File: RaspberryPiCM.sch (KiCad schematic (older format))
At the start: 16 parts

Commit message: [modified:] RTC revision [add:] RPis second I2C port
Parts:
- removed C?: 1uF, Capacitor_SMD:C_0603_1608Metric, symbol Device:C
- added C?: 1uF, symbol Device:C
- added C?: 100nF, symbol Device:C
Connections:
- net +3V3: now also C?.1, C?.1
- net Earth: now also C?.2, C?.2; no longer BT?.2 (-), U?.10 (GND), U?.11 (GND), U?.12 (GND), U?.13 (GND), U?.5 (GND), U?.6 (GND), U?.7 (GND), U?.8 (GND), U?.9 (GND)
- net GND: now also BT?.2 (-), U?.10 (GND), U?.11 (GND), U?.12 (GND), U?.13 (GND), U?.5 (GND), U?.6 (GND), U?.7 (GND), U?.8 (GND), U?.9 (GND)
- net Rpi.SCL1: now also U?.15 (SDA); no longer U?.16 (SCL)
- net Rpi.SDA1: now also U?.16 (SCL); no longer U?.15 (SDA)
- net Rpi.SDA0: now reaches MD?.3 (GPIO0)
- net Rpi.SCL0: now reaches MD?.5 (GPIO1)
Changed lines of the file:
@@
 NoConn ~ 5700 750
 NoConn ~ 5700 7500
-Text Label 1450 1350 2    50   ~ 0
+Text Label 1800 1350 2    50   ~ 0
 Rpi.SDA1
-Text Label 1450 1500 2    50   ~ 0
+Text Label 1800 1500 2    50   ~ 0
 Rpi.SCL1
 Text Label 1050 6150 0    50   ~ 0
@@
 AR Path="/60ED0E56" Ref="U?"  Part="1"
 AR Path="/614D7E9D/60ED0E56" Ref="U?"  Part="1"
-F 0 "U?" H 18900 2561 50  0000 C CNN
-F 1 "DS3231M" H 18900 2470 50  0000 C CNN
+F 0 "U?" H 18800 3000 50  0000 C CNN
+F 1 "DS3231M" H 18900 3100 50  0000 C CNN
 F 2 "Package_SO:SOIC-16W_7.5x10.3mm_P1.27mm" H 18900 2450 50  0001 C CNN
 F 3 "http://datasheets.maximintegrated.com/en/ds/DS3231.pdf" H 19170 3100 50  0001 C CNN
@@
 Wire Wire Line
 	19900 2550 19900 2750
-Wire Wire Line
-	19900 3150 19900 3550
-Wire Wire Line
-	19900 3550 18900 3550
-Wire Wire Line
-	18900 3550 18900 3450
 NoConn ~ 19400 2850
 NoConn ~ 19400 3150
@@
 	1    0    0    -1
 $EndComp
-Wire Wire Line
-	18800 2350 18800 2450
-$Comp
-L Device:C C?
-U 1 1 60ED0E72
-P 18550 2450
-F 0 "C?" V 18298 2450 50  0000 C CNN
-F 1 "1uF" V 18389 2450 50  0000 C CNN
-F 2 "Capacitor_SMD:C_0603_1608Metric" H 18588 2300 50  0001 C CNN
-F 3 "~" H 18550 2450 50  0001 C CNN
-	1    18550 2450
-	0    1    1    0
-$EndComp
 $Comp
 L power:Earth #PWR?
 U 1 1 60ED0E78
-P 18100 2500
-F 0 "#PWR?" H 18100 2250 50  0001 C CNN
-F 1 "Earth" H 18100 2350 50  0001 C CNN
-F 2 "" H 18100 2500 50  0001 C CNN
-F 3 "~" H 18100 2500 50  0001 C CNN
-	1    18100 2500
-	1    0    0    -1
-$EndComp
+P 18100 2600
+F 0 "#PWR?" H 18100 2350 50  0001 C CNN
+F 1 "Earth" H 18100 2450 50  0001 C CNN
+F 2 "" H 18100 2600 50  0001 C CNN
+F 3 "~" H 18100 2600 50  0001 C CNN
+	1    18100 2600
+	1    0    0    -1
+$EndComp
+Text Label 1800 900  2    50   ~ 0
+Rpi.SDA0
+Text Label 1800 1050 2    50   ~ 0
+Rpi.SCL0
+Wire Wire Line
+	1450 900  3700 900
+Wire Wire Line
+	1450 1050 3700 1050
+Entry Wire Line
+	1350 800  1450 900
+Entry Wire Line
+	1350 950  1450 1050
+Wire Bus Line
+	1000 800  1350 800
+Text HLabel 1000 800  0    50   BiDi ~ 0
+I2C_0
+Wire Bus Line
+	1350 800  1350 950
+Entry Wire Line
+	1350 1250 1450 1350
+Entry Wire Line
+	1350 1400 1450 1500
+Wire Bus Line
+	1000 1250 1350 1250
+Text HLabel 1000 1250 0    50   BiDi ~ 0
+I2C_1
+Wire Bus Line
+	1350 1250 1350 1400
+Text Label 17200 2850 2    50   ~ 0
+Rpi.SDA1
+Text Label 17200 2950 2    50   ~ 0
+Rpi.SCL1
+Entry Wire Line
+	16750 2750 16850 2850
+Entry Wire Line
+	16750 2850 16850 2950
+Wire Bus Line
+	16400 2750 16750 2750
+Text HLabel 16400 2750 0    50   BiDi ~ 0
+I2C_1
+Wire Bus Line
+	16750 2850 16750 2750
+Wire Wire Line
+	16850 2950 18400 2950
+Wire Wire Line
+	16850 2850 18400 2850
+$Comp
+L Device:C C?
+U 1 1 60E7A24B
+P 18100 2300
+F 0 "C?" H 18215 2346 50  0000 L CNN
+F 1 "1uF" H 18215 2255 50  0000 L CNN
+F 2 "" H 18138 2150 50  0001 C CNN
+F 3 "~" H 18100 2300 50  0001 C CNN
+	1    18100 2300
+	1    0    0    -1
+$EndComp
+Wire Wire Line
+	18800 2350 18800 2650
+$Comp
+L power:+3.3V #PWR?
+U 1 1 60E94ADC
+P 18100 2000
+F 0 "#PWR?" H 18100 1850 50  0001 C CNN
+F 1 "+3.3V" H 18115 2173 50  0000 C CNN
+F 2 "" H 18100 2000 50  0001 C CNN
+F 3 "" H 18100 2000 50  0001 C CNN
+	1    18100 2000
+	1    0    0    -1
+$EndComp
+Wire Wire Line
+	18100 2000 18100 2150
+Wire Wire Line
+	18100 2450 18100 2600
+Text Notes 18750 1800 0    50   ~ 0
+Clock
 $Comp
 L power:Earth #PWR?
-U 1 1 60ED0E7E
+U 1 1 60ED5A08
+P 17650 2600
+F 0 "#PWR?" H 17650 2350 50  0001 C CNN
+F 1 "Earth" H 17650 2450 50  0001 C CNN
+F 2 "" H 17650 2600 50  0001 C CNN
+F 3 "~" H 17650 2600 50  0001 C CNN
+	1    17650 2600
+	1    0    0    -1
+$EndComp
+$Comp
+L Device:C C?
+U 1 1 60ED5A0E
+P 17650 2300
+F 0 "C?" H 17765 2346 50  0000 L CNN
+F 1 "100nF" H 17765 2255 50  0000 L CNN
+F 2 "" H 17688 2150 50  0001 C CNN
+F 3 "~" H 17650 2300 50  0001 C CNN
+	1    17650 2300
+	1    0    0    -1
+$EndComp
+$Comp
+L power:+3.3V #PWR?
+U 1 1 60ED5A14
+P 17650 2000
+F 0 "#PWR?" H 17650 1850 50  0001 C CNN
+F 1 "+3.3V" H 17665 2173 50  0000 C CNN
+F 2 "" H 17650 2000 50  0001 C CNN
+F 3 "" H 17650 2000 50  0001 C CNN
+	1    17650 2000
+	1    0    0    -1
+$EndComp
+Wire Wire Line
+	17650 2000 17650 2150
+Wire Wire Line
+	17650 2450 17650 2600
+$Comp
+L power:GND #PWR?
+U 1 1 60EEF8C1
 P 19900 3700
 F 0 "#PWR?" H 19900 3450 50  0001 C CNN
-F 1 "Earth" H 19900 3550 50  0001 C CNN
+F 1 "GND" H 19905 3527 50  0000 C CNN
 F 2 "" H 19900 3700 50  0001 C CNN
-F 3 "~" H 19900 3700 50  0001 C CNN
+F 3 "" H 19900 3700 50  0001 C CNN
 	1    19900 3700
 	1    0    0    -1
 $EndComp
 Wire Wire Line
-	19900 3700 19900 3550
-Connection ~ 19900 3550
-Wire Wire Line
-	18800 2450 18700 2450
-Connection ~ 18800 2450
-Wire Wire Line
-	18800 2450 18800 2650
-Wire Wire Line
-	18400 2450 18100 2450
-Wire Wire Line
-	18100 2450 18100 2500
-Text Label 17850 2950 2    50   ~ 0
-Rpi.SDA1
-Text Label 17850 2850 2    50   ~ 0
-Rpi.SCL1
-Wire Wire Line
-	18400 2950 17850 2950
-Wire Wire Line
-	17850 2850 18400 2850
-Wire Notes Line
-	20350 1900 20350 4150
-Wire Notes Line
-	20350 4150 17400 4150
-Wire Notes Line
-	17400 4150 17400 1900
-Wire Notes Line
-	17400 1900 20350 1900
-Text Notes 17600 2150 0    50   ~ 0
-Clock
+	19900 3150 19900 3700
+$Comp
+L power:GND #PWR?
+U 1 1 60EFCF13
+P 18900 3700
+F 0 "#PWR?" H 18900 3450 50  0001 C CNN
+F 1 "GND" H 18905 3527 50  0000 C CNN
+F 2 "" H 18900 3700 50  0001 C CNN
+F 3 "" H 18900 3700 50  0001 C CNN
+	1    18900 3700
+	1    0    0    -1
+$EndComp
+Wire Wire Line
+	18900 3450 18900 3700
 Wire Bus Line
 	900  5450 900  6050

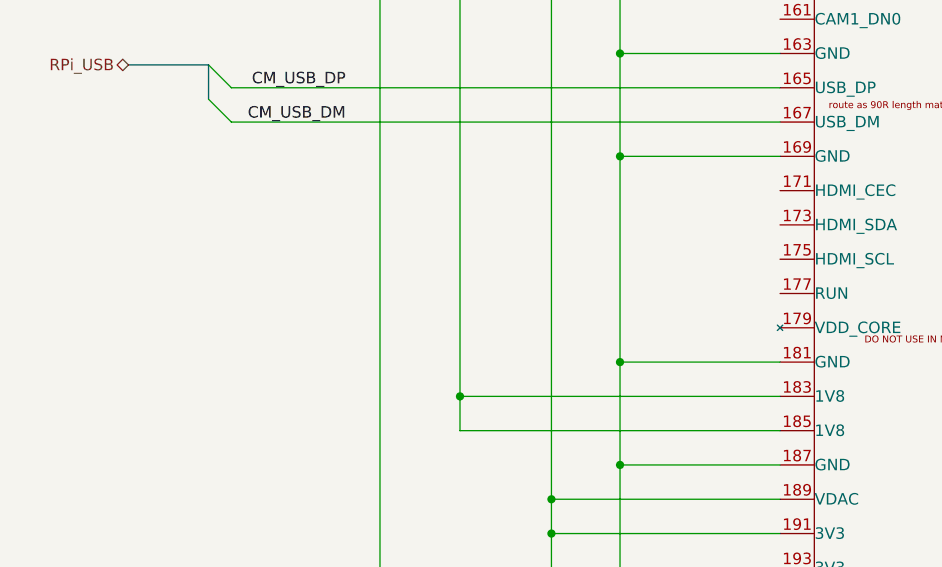
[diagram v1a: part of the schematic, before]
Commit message: [added:] 5V buck converter enable circuit [added:] RPi power up circuit
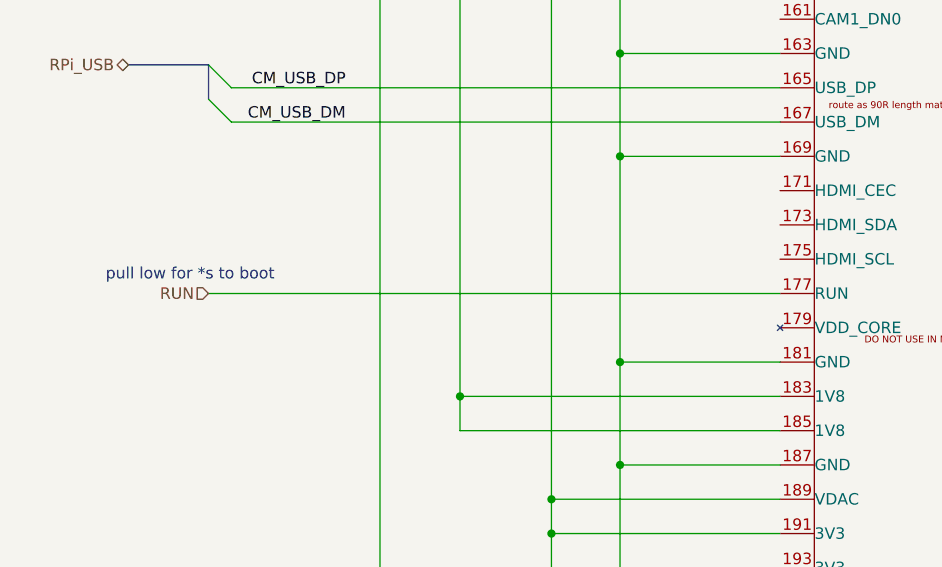
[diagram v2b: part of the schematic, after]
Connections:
- net RUN: now reaches MD?.177 (RUN)
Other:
- note added: "pull low for *s to boot"
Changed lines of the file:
@@
 Wire Wire Line
 	18900 3450 18900 3700
+Text HLabel 1200 14100 0    50   Input ~ 0
+RUN
+Wire Wire Line
+	1200 14100 3700 14100
+Text Notes 750  14050 0    50   ~ 0
+pull low for *s to boot
 Wire Bus Line
 	900  5450 900  6050
